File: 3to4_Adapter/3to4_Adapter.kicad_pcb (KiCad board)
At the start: 2 copper layers, 61 x 61 mm, 13 parts, among them J1 v3 Header, J2 v4 Header, J3 CLK_GND, U1 AMS1117-3.3

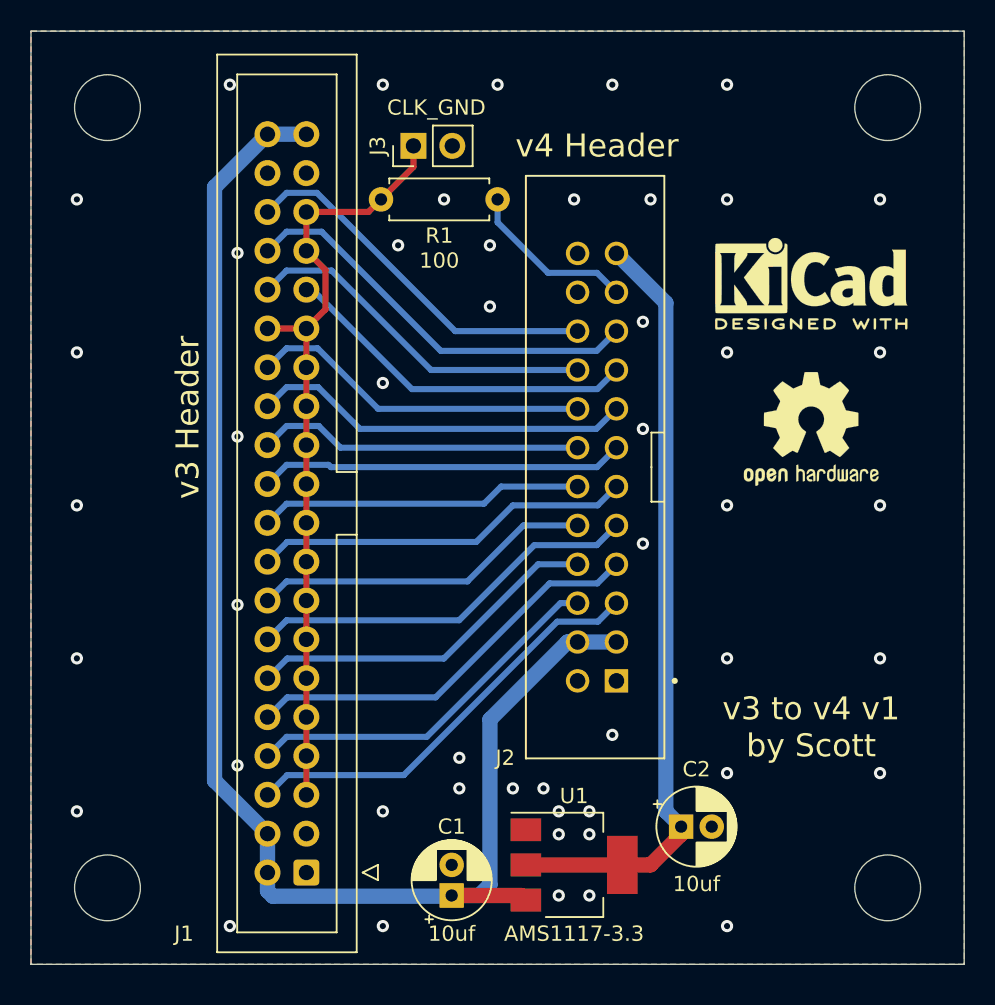
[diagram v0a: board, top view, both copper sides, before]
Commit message: added 3.3v jumper
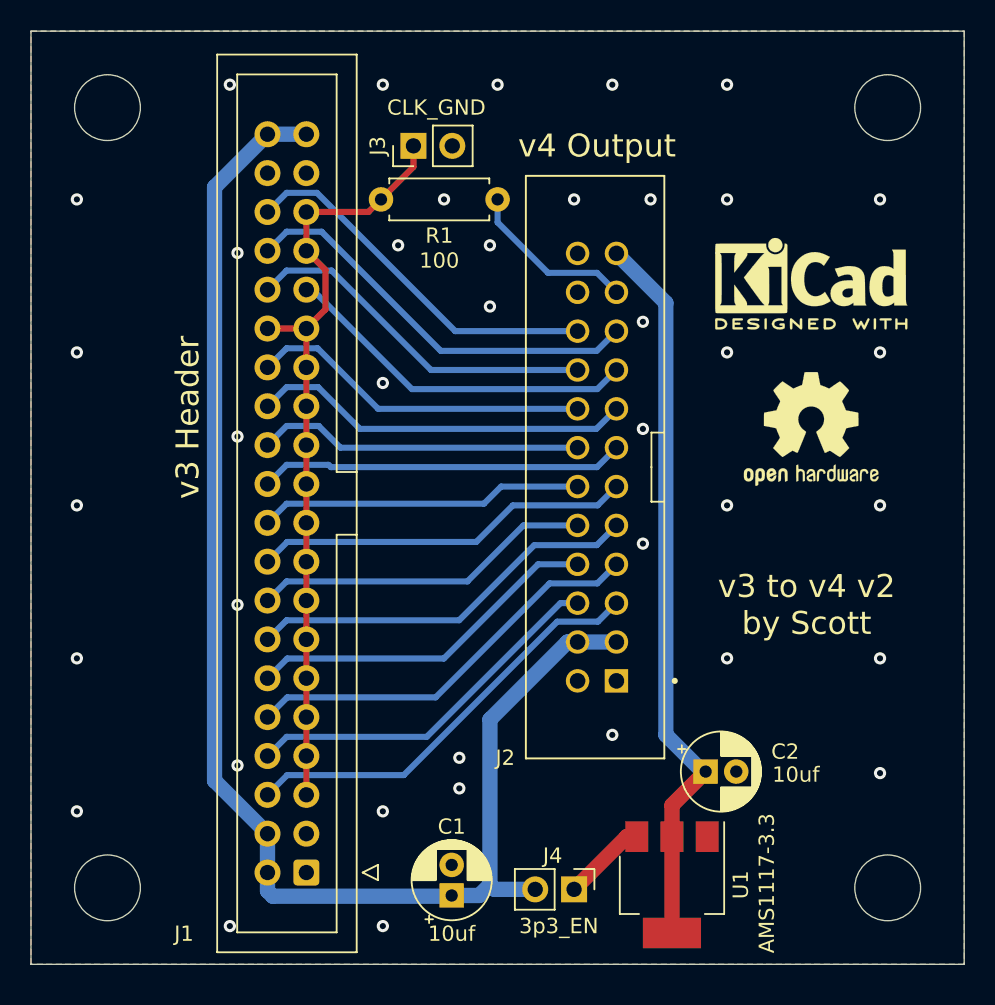
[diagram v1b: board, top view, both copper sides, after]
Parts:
- added J4: 3p3_EN, Connector_PinHeader_2.54mm:PinHeader_1x02_P2.54mm_Vertical, F.Cu at (147.5, 130.1)
- J2: value v4 Header -> v4 Output
- moved U1 6.53 mm to (153.9, 129.8), turned to 270 degrees
- moved C2 3.94 mm to (156.1, 122.4)
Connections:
- U1 pad 3: +5V -> /3p_IN
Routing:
- net /3p_IN: track 0.00 -> 5.53 mm
- net +3V3: track 50.7 -> 47.9 mm
- net +5V: track 96.0 -> 94.1 mm
- net GND: vias 49 -> 39
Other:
- board text added: "v3 to v4 v2 by Scott"
- board text removed: "v3 to v4 v1 by Scott"

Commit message: swapped header
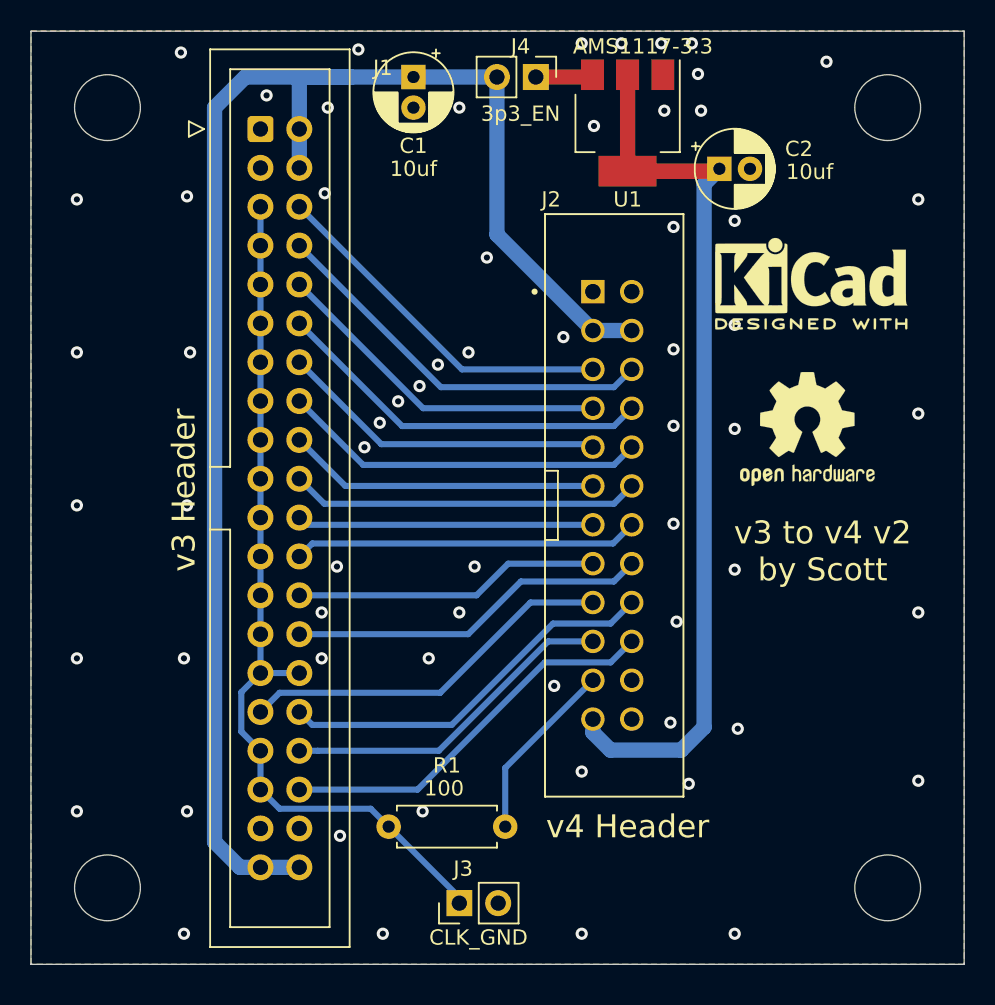
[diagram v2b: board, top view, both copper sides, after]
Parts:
- J2: value v4 Output -> v4 Header
- moved C1 53.6 mm to (137.0, 77.0), turned to 270 degrees
- moved J4 53.2 mm to (145.0, 77.0)
- moved U1 49.9 mm to (151.0, 80.0)
- moved J3 49.6 mm to (140.0, 131.0)
- moved J1 48.7 mm to (127.0, 80.4), turned to 0 degrees
- moved R1 41.0 mm to (143.0, 126.0)
- moved C2 39.4 mm to (157.0, 83.0)
- moved J2 2.69 mm to (150.0, 105.0), turned to 270 degrees
- moved REF** 0.25 mm to (162.8, 100.0)
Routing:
- net +3V3: track 47.9 -> 58.5 mm
- net +5V: track 94.1 -> 104.6 mm
- net CLK_V3: track 51.3 -> 58.0 mm
- net OUT11: track 25.0 -> 20.0 mm
- net OUT15: track 27.1 -> 22.2 mm
- net OUT9: track 23.9 -> 19.4 mm
- net OUT1: track 28.0 -> 23.6 mm
- net OUT5: track 25.9 -> 21.5 mm
- net OUT7: track 24.8 -> 20.4 mm
- net OUT3: track 26.9 -> 22.5 mm
- net OUT14: track 23.5 -> 25.4 mm
- net /3p_IN: track 5.53 -> 3.76 mm
- net OUT2: track 24.4 -> 26.0 mm
- net OUT6: track 22.3 -> 23.9 mm
- net OUT4: track 23.4 -> 25.0 mm
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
